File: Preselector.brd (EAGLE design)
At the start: 160 x 100 mm, 134 parts, among them IC58 LMZ31707RVQ, Q2 FDV303N, X1 0733660061, X2 0733660061, X3 0733660061, X4 0733660061, X5 0733660061, X6 0733660061, X7 0733660061, X8 0733660061

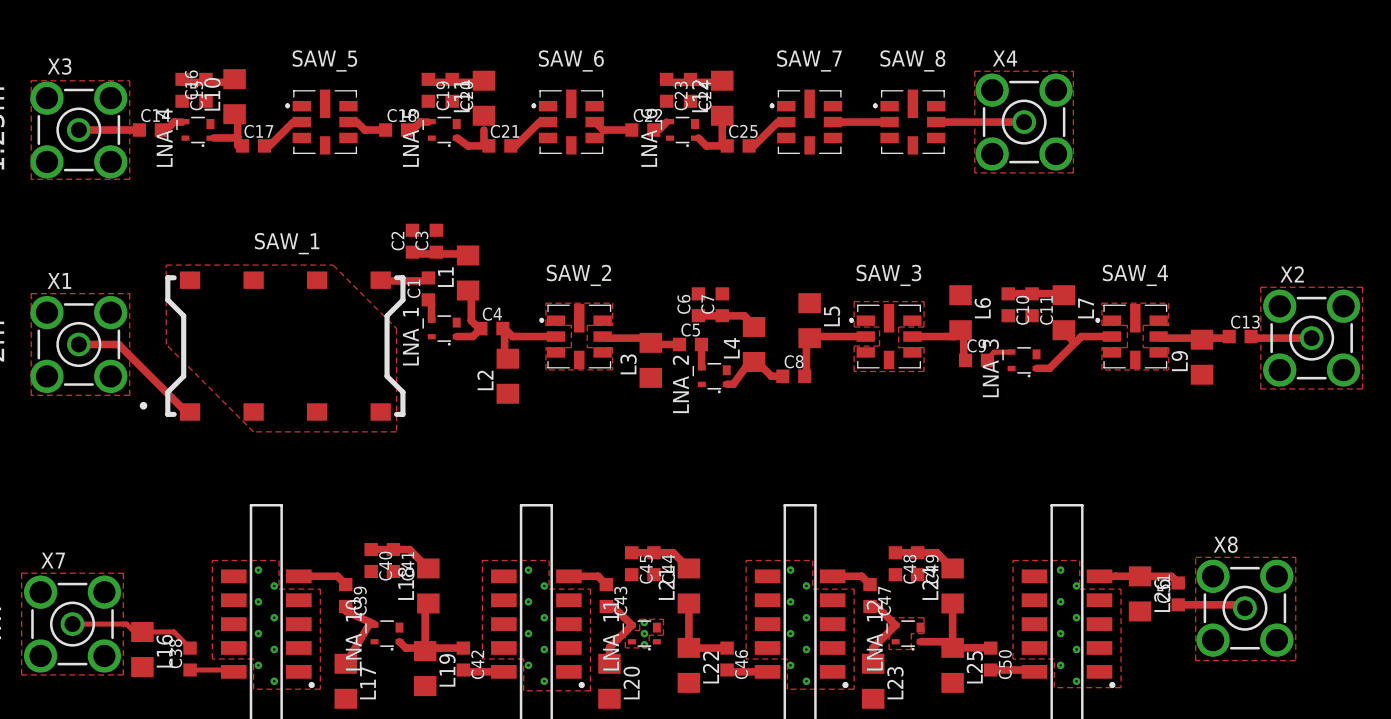
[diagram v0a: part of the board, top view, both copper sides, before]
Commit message: Kenneth, I redid the 1.25m and 2m band, replaced the wire with the route. The 4m band, I put the capacitors 44 and 45 in order, originally they were in 45 then 44 order. Other than that, the board seems to accurately represent the schematic. If you can take a look at it when you can, that'd be great. Let me know what you think and if any other changes should be made.
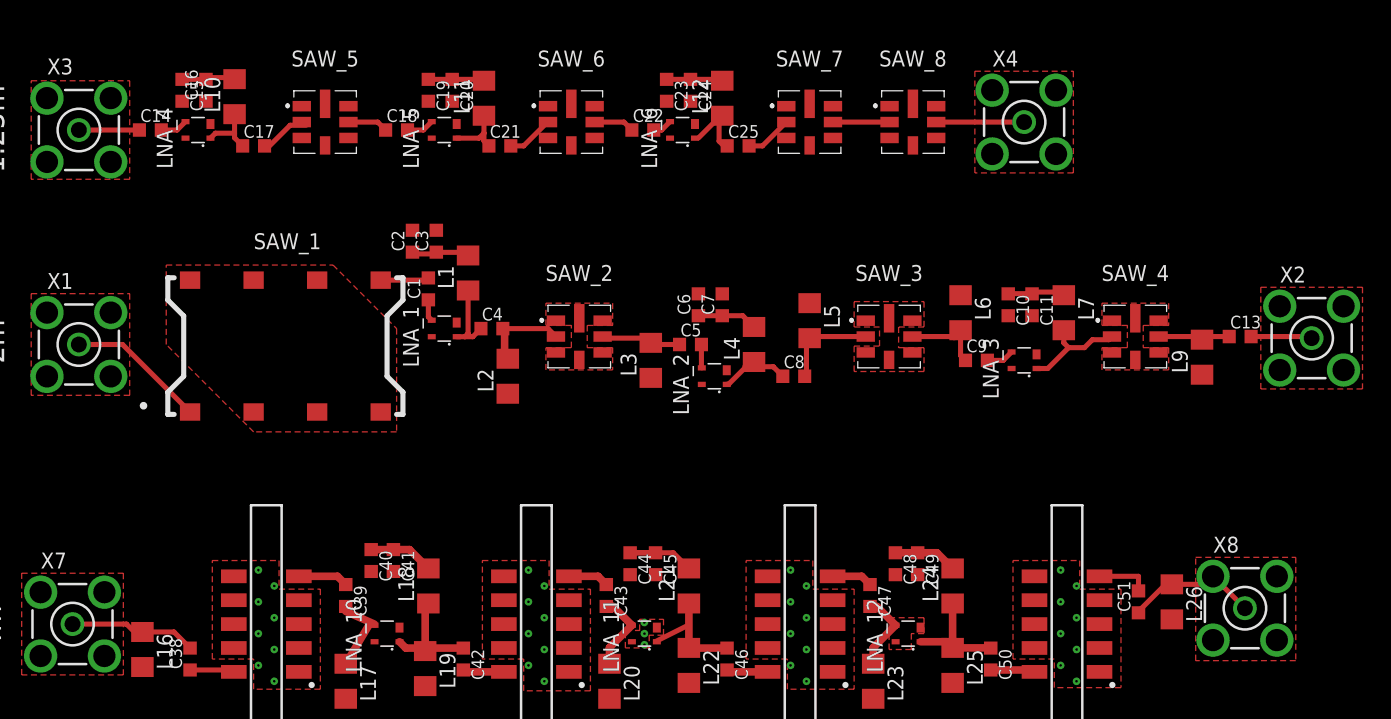
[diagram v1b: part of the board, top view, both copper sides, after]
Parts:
- moved C51 3.24 mm to (93.9, 14.0)
- moved L26 2.62 mm to (96.5, 14.0)
- moved C44 1.91 mm to (53.2, 17.0)
- moved C45 1.90 mm to (55.2, 17.0)
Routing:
- net 2M_RF_IN: track 45.3 -> 73.5 mm
- net +5V3: track 15.4 -> 35.4 mm
- net 1.25M_RF_IN: track 0.00 -> 9.81 mm
- net N$27: track 8.17 -> 0.00 mm
- net 1.25M_RF_IN3: track 0.00 -> 5.45 mm
- net N$28: track 5.33 -> 0.00 mm
- net N$11: track 4.89 -> 0.00 mm
- net N$14: track 0.00 -> 4.52 mm
- net N$40: track 4.45 -> 0.00 mm
- net N$7: track 3.81 -> 0.00 mm
- net 1.25M_RF_IN_1: track 0.00 -> 3.76 mm
- net N$33: track 3.63 -> 0.00 mm
- net 1.25M_RF_IN_: track 0.00 -> 3.36 mm
- net N$23: track 4.02 -> 0.72 mm
- net 1.2M5_RF_IN4: track 0.00 -> 3.24 mm
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
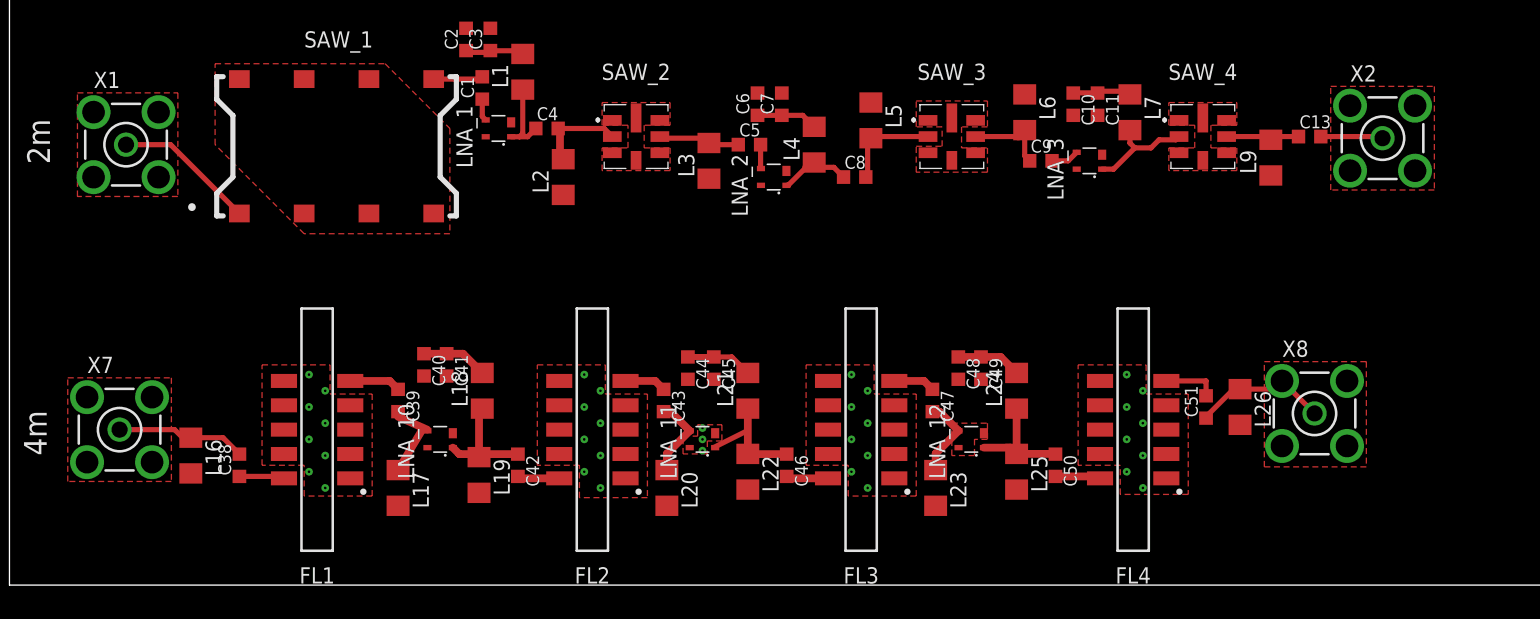
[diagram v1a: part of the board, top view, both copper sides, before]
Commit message: Renamed 4m net, look at the naming convention on there to continue. I also renamed the beginning of the 2m band, I'm renaming the 5v3 net to just +5v. I think the voltage can be the same name because it will connect to a power plane.
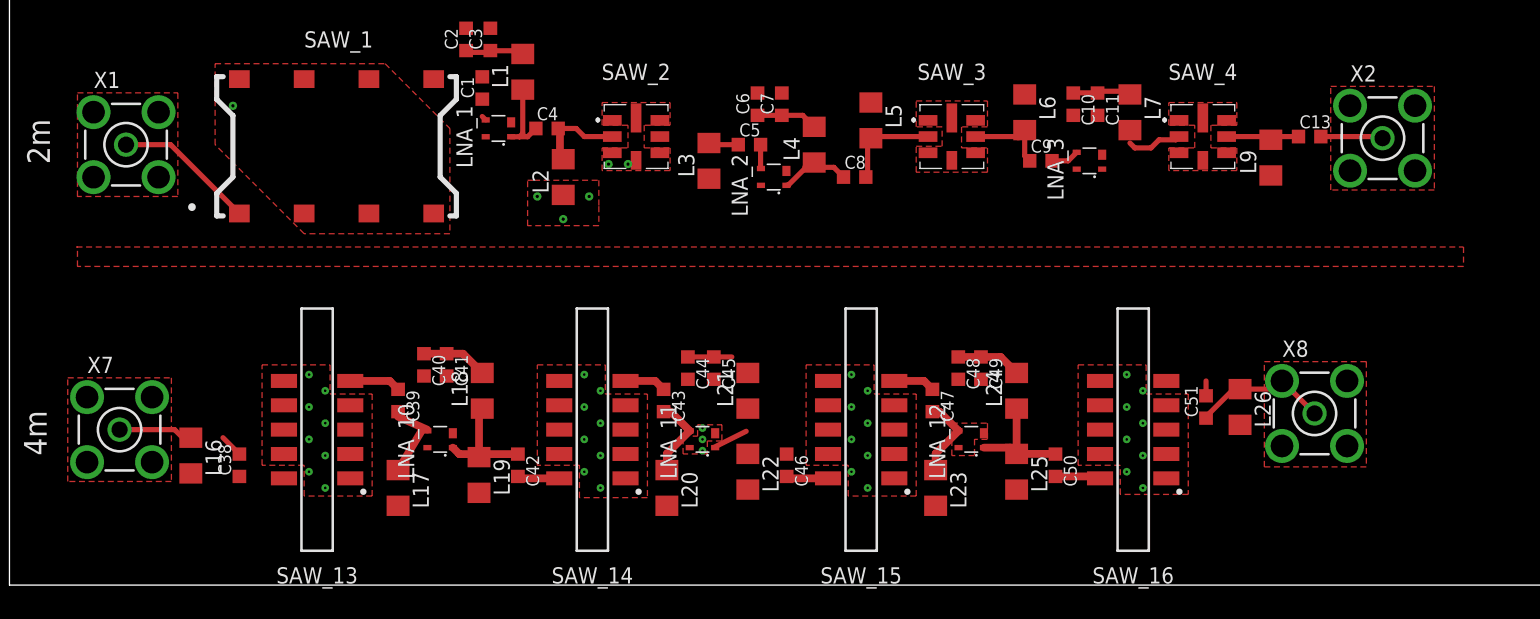
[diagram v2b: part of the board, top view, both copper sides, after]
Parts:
- renumbered FL1 to SAW_13, FL2 to SAW_14, FL3 to SAW_15, FL4 to SAW_16
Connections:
- net 4M_RF_IN1 renamed SAW_14_OUT
- removed net GND3: L12.1
- removed net N$2: C13.2, X2.1
- new net +5V: C40.1, C41.1, C44.1, C45.1, L18.2, L21.2
- new net 2M_RF_IN_14: C1.2, LNA_1.3
- new net 2M_RF_IN_2: C4.1, L1.1, LNA_1.1
- new net 2M_RF_IN_3: C4.2, L2.2, SAW_2.2
- new net 2M_RF_IN_4: C5.1, L3.2, SAW_2.6
- new net 2M_RF_IN_5: C5.2, LNA_2.3
- new net 2M_RF_IN_6: C8.1, L4.1, LNA_2.1
- new net 2M_RF_IN_7: C8.2, L5.2, SAW_3.2
- new net 2M_RF_IN_9: C9.1, L6.2, SAW_3.6
- new net 4M_RF_OUT: C51.2, L26.1, X8.1
- new net LNA_10_IN: C39.2, L17.1, LNA_10.3
- new net LNA_10_OUT: C42.1, L18.1, L19.1, LNA_10.1
- new net LNA_11_IN: C43.2, L20.1, LNA_11.3
- new net LNA_11_OUT: C46.1, L21.1, L22.1, LNA_11.1
- new net LNA_12_IN: C47.2, L23.1, LNA_12.3
- new net LNA_12_OUT: C50.1, L24.1, L25.1, LNA_12.1
- new net LNA_3_IN: C12.1, L7.2, LNA_3.1
- new net LNA_3_OUT: C9.2, LNA_3.3
- new net SAW_13_IN: C38.2, SAW_13.10
- new net SAW_13_OUT: C39.1, SAW_13.5
- new net SAW_14_IN: C42.2, SAW_14.10
- new net SAW_15_IN: C46.2, SAW_15.10
- new net SAW_15_OUT: C47.1, SAW_15.5
- new net SAW_16_IN: C50.2, SAW_16.10
- new net SAW_16_OUT: C51.1, SAW_16.5
- new net SAW_1_OUT: C1.1, SAW_1.8
- new net SAW_4_IN: C13.1, L9.2, SAW_4.6
- new net SAW_4_OUT: C12.2, L8.2, SAW_4.2
- net +5V3: no longer C40.1, C41.1, C44.1, C45.1, L18.2, L21.2
- net 2M_RF_IN: now also C13.2, X2.1; no longer C1.1, C1.2, C12.1, C12.2, C13.1, C4.1, C4.2, C5.1, C5.2, C8.1, C8.2, C9.1, C9.2, L1.1, L2.2, L3.2, L4.1, L5.2, L6.2, L7.2, L8.2, L9.2, LNA_1.1, LNA_1.3, LNA_2.1, LNA_2.3, LNA_3.1, LNA_3.3, SAW_1.8, SAW_2.2, SAW_2.6, SAW_3.2, SAW_3.6, SAW_4.2, SAW_4.6
- net 4M_RF_IN: no longer C38.2, C39.1, C39.2, C42.1, C42.2, C43.2, C46.1, C46.2, C47.1, C47.2, C50.1, C50.2, C51.1, C51.2, L17.1, L18.1, L19.1, L20.1, L21.1, L22.1, L23.1, L24.1, L25.1, L26.1, LNA_10.1, LNA_10.3, LNA_11.1, LNA_11.3, LNA_12.1, LNA_12.3, SAW_13.10, SAW_13.5, SAW_14.10, SAW_15.10, SAW_15.5, SAW_16.10, SAW_16.5, X8.1
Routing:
- net 4M_RF_IN: track 89.4 -> 5.40 mm
- net 2M_RF_IN: track 73.5 -> 16.0 mm
- net +5V3: track 35.4 -> 22.9 mm
- net LNA_12_OUT: track 0.00 -> 9.37 mm
- net LNA_10_OUT: track 0.00 -> 9.22 mm
- net +5V: track 0.00 -> 8.64 mm
- net 4M_RF_OUT: track 0.00 -> 7.80 mm
- net 2M_RF_IN_7: track 0.00 -> 7.62 mm
- net 2M_RF_IN_3: track 0.00 -> 7.10 mm
- net LNA_10_IN: track 0.00 -> 6.60 mm
- net LNA_11_IN: track 0.00 -> 6.49 mm
- net LNA_12_IN: track 0.00 -> 6.49 mm
- net 2M_RF_IN_9: track 0.00 -> 6.33 mm
- net 2M_RF_IN_2: track 0.00 -> 6.01 mm
- net SAW_4_IN: track 0.00 -> 5.85 mm
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- added copper zone on layer 2, net GND

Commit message: Added connectors on 4m band and also copied LDO over
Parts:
- removed X7, X8: 0733660061, con-coax:BU-SMA-V
- added +5V14: TPTP20SQ, testpad:TP20SQ
- added C52, C72: NFM21PS106B0J3D, DEEP EDDY:NFM21PS
- added C57, C73: 470n, rcl:C0402K
- added IC4: TPS7A8101DRB, DEEP EDDY:DRB
- added R17: 52.3k, rcl:R0603
- added R18, R20: 10.0k, rcl:R0603
- added X25, X26, X27, X28, X29, X30, X31, X32: 0733660061, con-coax:BU-SMA-V
- moved SAW_16 60.6 mm to (148.7, 12.8)
- moved C51 60.6 mm to (154.4, 14.6)
- moved L26 60.6 mm to (157.1, 14.6)
- moved C48 51.8 mm to (126.1, 13.8)
- moved C47 51.8 mm to (124.1, 11.3)
- moved C49 51.8 mm to (127.9, 13.8)
- moved C50 51.8 mm to (133.7, 6.22)
- moved L23 51.8 mm to (124.3, 4.45)
- moved L24 51.8 mm to (130.7, 12.1)
- moved L25 51.8 mm to (130.7, 5.71)
- moved LNA_12 51.8 mm to (127.1, 8.26)
- moved SAW_15 41.5 mm to (108.3, 12.8)
- moved L20 31.3 mm to (82.7, 4.45)
- moved C43 31.3 mm to (82.4, 11.3)
- moved C44 31.3 mm to (84.3, 13.8)
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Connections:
- new net +5V0A: +5V14.TP, C72.OUT, C73.2, R17.1
- new net N$2: C73.1, IC4.3, R17.2, R18.1
- new net N$3: C57.1, IC4.6
- new net N$4: C52.OUT, IC4.7, IC4.8
- new net N$6: C72.IN, IC4.1, IC4.2
- new net PRE_PWR: IC4.5, R20.2
- net +5V3: now also C52.IN, R20.1
- net 4M_RF_IN: now also X25.1; no longer X7.1
- net 4M_RF_OUT: now also X32.1; no longer X8.1
- net GND: now also C52.GND1, C52.GND2, C52.GND3, C52.GND4, C52.GND5, C52.GND6, C52.GND7, C52.GND8, C57.2, C72.GND1, C72.GND2, C72.GND3, C72.GND4, C72.GND5, C72.GND6, C72.GND7, C72.GND8, IC4.4, IC4.P1, IC4.P2, IC4.P3, IC4.P4, IC4.P5, IC4.PAD, R18.2, X25.2, X25.3, X25.4, X25.5, X26.2, X26.3, X26.4, X26.5, X27.2, X27.3, X27.4, X27.5, X28.2, X28.3, X28.4, X28.5, X29.2, X29.3, X29.4, X29.5, X30.2, X30.3, X30.4, X30.5, X31.2, X31.3, X31.4, X31.5, X32.2, X32.3, X32.4, X32.5; no longer X7.2, X7.3, X7.4, X7.5, X8.2, X8.3, X8.4, X8.5
- net SAW_13_OUT: now also X26.1
- net SAW_14_IN: now also X27.1
- net SAW_14_OUT: now also X28.1
- net SAW_15_IN: now also X29.1
- net SAW_15_OUT: now also X30.1
- net SAW_16_IN: now also X31.1
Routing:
- net LNA_12_OUT: track 9.37 -> 0.02 mm
- net LNA_10_OUT: track 9.22 -> 0.36 mm
- net +5V: track 8.64 -> 0.00 mm
- net 4M_RF_OUT: track 7.80 -> 0.00 mm
- net LNA_10_IN: track 6.60 -> 0.00 mm
- net LNA_11_IN: track 6.49 -> 0.00 mm
- net LNA_12_IN: track 6.49 -> 0.55 mm
- net 4M_RF_IN: track 5.40 -> 0.00 mm
- net +5V3: track 22.9 -> 17.9 mm
- net SAW_13_OUT: track 4.02 -> 0.00 mm
- net SAW_16_IN: track 3.56 -> 0.21 mm
- net SAW_15_IN: track 3.30 -> 0.00 mm
- net SAW_14_IN: track 3.30 -> 0.00 mm
- net SAW_14_OUT: track 3.26 -> 0.00 mm
- net SAW_15_OUT: track 3.26 -> 0.00 mm
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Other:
- board size 160 x 100 mm -> 175.3 x 123.8 mm

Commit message: Connected the connectors (schematic). Ripped up traces from board.
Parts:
- added X10, X11, X12, X13, X14, X15, X16, X17, X18, X19, X20, X21, X22, X23, X24, X7, X8, X9: 0733660061, con-coax:BU-SMA-V
- moved X6 671.5 mm to (-79.2, -564.4)
- moved X5 627.9 mm to (-79.2, -532.4)
- moved X4 596.2 mm to (-79.2, -500.4)
- moved X3 547.7 mm to (-79.2, -468.4)
- moved X2 526.3 mm to (-79.2, -436.4)
- moved C12 149.9 mm to (91.4, 52.1)
- moved L8 113.8 mm to (92.7, 56.6), turned to 90 degrees
- moved C13 4.58 mm to (107.2, 55.2)
- moved L9 4.58 mm to (104.1, 53.6)
- moved SAW_4 4.33 mm to (98.6, 55.2)
- moved L6 3.81 mm to (80.3, 53.6)
- moved C9 2.84 mm to (84.1, 54.9)
- moved L7 2.54 mm to (88.5, 54.9)
- moved LNA_3 1.27 mm to (85.3, 52.3)
- moved C10 0.36 mm to (84.3, 58.3)
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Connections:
- net 2M_RF_IN_2 renamed 2M_RF_IN17
- net 2M_RF_IN_5 renamed N$9
- net LNA_3_IN renamed 2M_RF_IN20
- removed net 1.25M_RF_IN_: C21.2, SAW_6.2
- removed net 1.25M_RF_IN_1: C25.2, SAW_7.2
- removed net 1.2M5_RF_IN4: C22.1, SAW_6.6
- removed net 2M_RF_IN_3: C4.2, L2.2, SAW_2.2
- removed net 2M_RF_IN_6: C8.1, L4.1, LNA_2.1
- removed net LNA_3_OUT: C9.2, LNA_3.3
- removed net N$14: SAW_7.6, SAW_8.2
- removed net N$15: C29.2, SAW_9.2
- removed net N$16: C30.1, SAW_9.5
- removed net N$17: C33.2, SAW_10.2
- removed net N$18: C34.1, SAW_10.5
- removed net N$19: C37.2, SAW_11.2
- removed net N$20: SAW_11.5, SAW_12.2
- removed net N$56: SAW_12.5, X6.1
- new net 2M_RF_IN1: C29.2, SAW_9.2, X18.1
- new net 2M_RF_IN10: C34.1, SAW_10.5, X21.1
- new net 2M_RF_IN11: SAW_11.5, SAW_12.2, X23.1
- new net 2M_RF_IN12: C17.2, SAW_5.2, X10.1
- new net 2M_RF_IN13: C21.2, SAW_6.2, X12.1
- new net 2M_RF_IN14: C22.1, SAW_6.6, X13.1
- new net 2M_RF_IN15: C25.2, SAW_7.2, X14.1
- new net 2M_RF_IN16: SAW_7.6, SAW_8.2, X15.1
- new net 2M_RF_IN19: C8.2, L4.1, LNA_2.1
- new net 2M_RF_IN5: C33.2, SAW_10.2, X20.1
- new net 2M_RF_IN7: C37.2, SAW_11.2, X22.1
- new net 2M_RF_IN9: C30.1, SAW_9.5, X19.1
- new net N$11: C9.1, L6.2, SAW_3.6, X6.1
- new net N$7: SAW_12.5, X24.1
- net 1.25M_RF_IN: no longer C17.2, SAW_5.2
- net 1.25M_RF_IN3: now also X11.1
- net 2M_RF_IN: now also X8.1; no longer X2.1
- net 2M_RF_IN2: now also X9.1; no longer X3.1
- net 2M_RF_IN3: now also X16.1; no longer X4.1
- net 2M_RF_IN4: now also X17.1; no longer X5.1
- net 2M_RF_IN_4: now also X4.1
- net 2M_RF_IN_7: now also C8.1, X5.1; no longer C8.2
- net 2M_RF_IN_9: now also C9.2, LNA_3.3; no longer C9.1, L6.2, SAW_3.6
- net GND: now also C4.2, L2.2, X10.2, X10.3, X10.4, X10.5, X11.2, X11.3, X11.4, X11.5, X12.2, X12.3, X12.4, X12.5, X13.2, X13.3, X13.4, X13.5, X14.2, X14.3, X14.4, X14.5, X15.2, X15.3, X15.4, X15.5, X16.2, X16.3, X16.4, X16.5, X17.2, X17.3, X17.4, X17.5, X18.2, X18.3, X18.4, X18.5, X19.2, X19.3, X19.4, X19.5, X20.2, X20.3, X20.4, X20.5, X21.2, X21.3, X21.4, X21.5, X22.2, X22.3, X22.4, X22.5, X23.2, X23.3, X23.4, X23.5, X24.2, X24.3, X24.4, X24.5, X3.1, X7.2, X7.3, X7.4, X7.5, X8.2, X8.3, X8.4, X8.5, X9.2, X9.3, X9.4, X9.5
- net SAW_1_OUT: now also X2.1
- net SAW_4_OUT: now also X7.1; no longer C12.2
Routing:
- net +5V3: track 17.9 -> 0.53 mm
- net 2M_RF_IN: track 16.0 -> 0.00 mm
- net 1.25M_RF_IN: track 9.81 -> 0.00 mm
- net 2M_RF_IN_7: track 7.62 -> 0.54 mm
- net 2M_RF_IN2: track 7.05 -> 0.00 mm
- net 2M_RF_IN_3: track 7.10 -> 0.18 mm
- net 2M_RF_IN3: track 6.35 -> 0.00 mm
- net 2M_RF_IN17: track 6.01 -> 0.00 mm
- net 2M_RF_IN_9: track 6.33 -> 0.54 mm
- net 1.25M_RF_IN3: track 5.45 -> 0.00 mm
- net SAW_4_IN: track 5.85 -> 0.71 mm
- net N$37: track 5.14 -> 0.00 mm
- net N$56: track 5.08 -> 0.00 mm
- net N$14: track 4.53 -> 0.00 mm
- net 2M_RF_IN4: track 4.45 -> 0.00 mm
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
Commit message: Aligned most rows. Added some vias and fixed the divider polygon that can be copied for other bands.
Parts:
- moved X7 689.9 mm to (148.3, 54.9)
- moved X6 651.3 mm to (122.7, 54.9)
- moved X5 615.4 mm to (104.6, 54.9)
- moved X4 577.7 mm to (80.3, 54.9)
- moved X3 542.3 mm to (63.2, 54.9)
- moved X15 519.0 mm to (127.5, 71.6), turned to 90 degrees
- moved X2 505.9 mm to (41.7, 54.9)
- moved X14 483.0 mm to (110.2, 71.9), turned to 90 degrees
- moved X13 445.0 mm to (88.4, 71.9), turned to 90 degrees
- moved X12 408.6 mm to (70.4, 71.9), turned to 90 degrees
- moved X11 370.9 mm to (48.5, 71.9), turned to 90 degrees
- moved X23 358.7 mm to (115.1, 89.2)
- moved X10 334.7 mm to (30.5, 71.9), turned to 90 degrees
- moved X21 313.0 mm to (80.0, 89.2)
- moved X22 273.6 mm to (101.3, 89.2)
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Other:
- board size 175.3 x 123.8 mm -> 183 x 123.8 mm
- board text added: "Aligned"
- board text added: "Misaligned by 5mil"

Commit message: started fixing some of the ERC errors in the schematic. DRC is for the board. Cut down on half of the errors and approved a few that were from the POWER SYSTEM page.
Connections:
- net 2M_RF_IN12 renamed SAW_5_IN
- net 2M_RF_IN13 renamed LNA_5_OUT
- new net LNA_4_OUT: C17.1, L10.1, LNA_4.1
- new net SAW_5_OUT: C18.1, SAW_5.6, X11.1
- net +5V: now also C10.1, C11.1, C15.1, C16.1, C19.1, C2.1, C20.1, C23.1, C24.1, C27.1, C28.1, C3.1, C31.1, C32.1, C35.1, C36.1, C48.1, C49.1, C6.1, C7.1, L1.2, L10.2, L11.2, L12.1, L13.2, L14.2, L15.2, L24.2, L4.2, L7.1
- net +5V3: no longer C10.1, C11.1, C15.1, C16.1, C19.1, C2.1, C20.1, C23.1, C24.1, C27.1, C28.1, C3.1, C31.1, C32.1, C35.1, C36.1, C48.1, C49.1, C6.1, C7.1, L1.2, L10.2, L11.2, L13.2, L14.2, L15.2, L24.2, L4.2, L7.1
- net 1.25M_RF_IN: now also C14.1, X9.1; no longer C17.1, L10.1, LNA_4.1
- net 1.25M_RF_IN3: no longer C18.1, SAW_5.6, X11.1
- net 2M_RF_IN2: no longer C14.1, X9.1
- net SAW_4_OUT: now also C12.2
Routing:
- net +5V3: track 0.53 -> 0.00 mm
- net +5V: track 0.00 -> 0.53 mm

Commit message: Fixed all ERC errors
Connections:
- net +5V renamed +5V0
- net 1.25M_RF_IN1 renamed LNA_6_IN
- net 1.25M_RF_IN3 renamed LNA_5_IN
- net 2M_RF_IN1 renamed SAW_9_IN
- net 2M_RF_IN10 renamed SAW_10_OUT
- net 2M_RF_IN11 renamed SAW_11_12_RF
- net 2M_RF_IN14 renamed SAW+6_OUT
- net 2M_RF_IN15 renamed SAW_7_IN
- net 2M_RF_IN16 renamed SAW_7_8_RF
- net 2M_RF_IN17 renamed LNA_1_OUT
- net 2M_RF_IN19 renamed LNA_2_OUT
- net 2M_RF_IN2 renamed LNA_4_IN
- net 2M_RF_IN20 renamed LNA_3_OUT
- net 2M_RF_IN3 renamed 1.25_RF_OUT
- net 2M_RF_IN5 renamed SAW_10_IN
- net 2M_RF_IN6 renamed LNA_8_IN
- net 2M_RF_IN7 renamed SAW_11_IN
- net 2M_RF_IN8 renamed LNA_9_IN
- net 2M_RF_IN9 renamed SAW_9_OUT
- net 2M_RF_IN_14 renamed LNA_1_IN
- net 2M_RF_IN_4 renamed SAW_2_OUT
- net 2M_RF_IN_7 renamed SAW_3_IN
- net 2M_RF_IN_9 renamed LNA_3_IN
- net GND5 renamed LNA_8_OUT
- net GND6 renamed LNA_9_OUT
- net N$11 renamed SAW_3_OUT
- net N$13 renamed LNA_6_OUT
- net N$7 renamed 70CM_RF_OUT
- net N$9 renamed LNA_2_IN
- removed net 2M_RF_IN4: C26.1, C26.2, LNA_7.3, X17.1
- new net 2M_RF_OUT: C13.2, X8.1
- new net LNA_7_IN: C26.2, LNA_7.3
- new net LNA_7_OUT: C29.1, L13.1, LNA_7.1
- new net SAW_2_IN: C4.2, L2.2, SAW_2.2, X3.1
- new net SAW_6_IN: C21.2, SAW_6.2, X12.1
- net 1.25M_RF_IN: no longer C21.1, L11.1, LNA_5.1
- net 2M_RF_IN: no longer C13.2, X8.1
- net 70CM_RF_IN: now also C26.1, X17.1; no longer C29.1, L13.1, LNA_7.1
- net GND: no longer C4.2, L2.2, X3.1
- net LNA_5_OUT: now also C21.1, L11.1, LNA_5.1; no longer C21.2, SAW_6.2, X12.1
- net SAW_4_IN: now also C12.2, L8.2, SAW_4.2, X7.1; no longer C13.1, L9.2, SAW_4.6
- net SAW_4_OUT: now also C13.1, L9.2, SAW_4.6; no longer C12.2, L8.2, SAW_4.2, X7.1
